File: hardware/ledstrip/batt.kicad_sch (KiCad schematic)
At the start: 37 parts, among them J4 BMS connectors, Q5 Q_NMOS, Q6 Q_NMOS, Q7 Q_NMOS, Q8 Q_NMOS, Q9 Q_PMOS, U5 BQ25703A

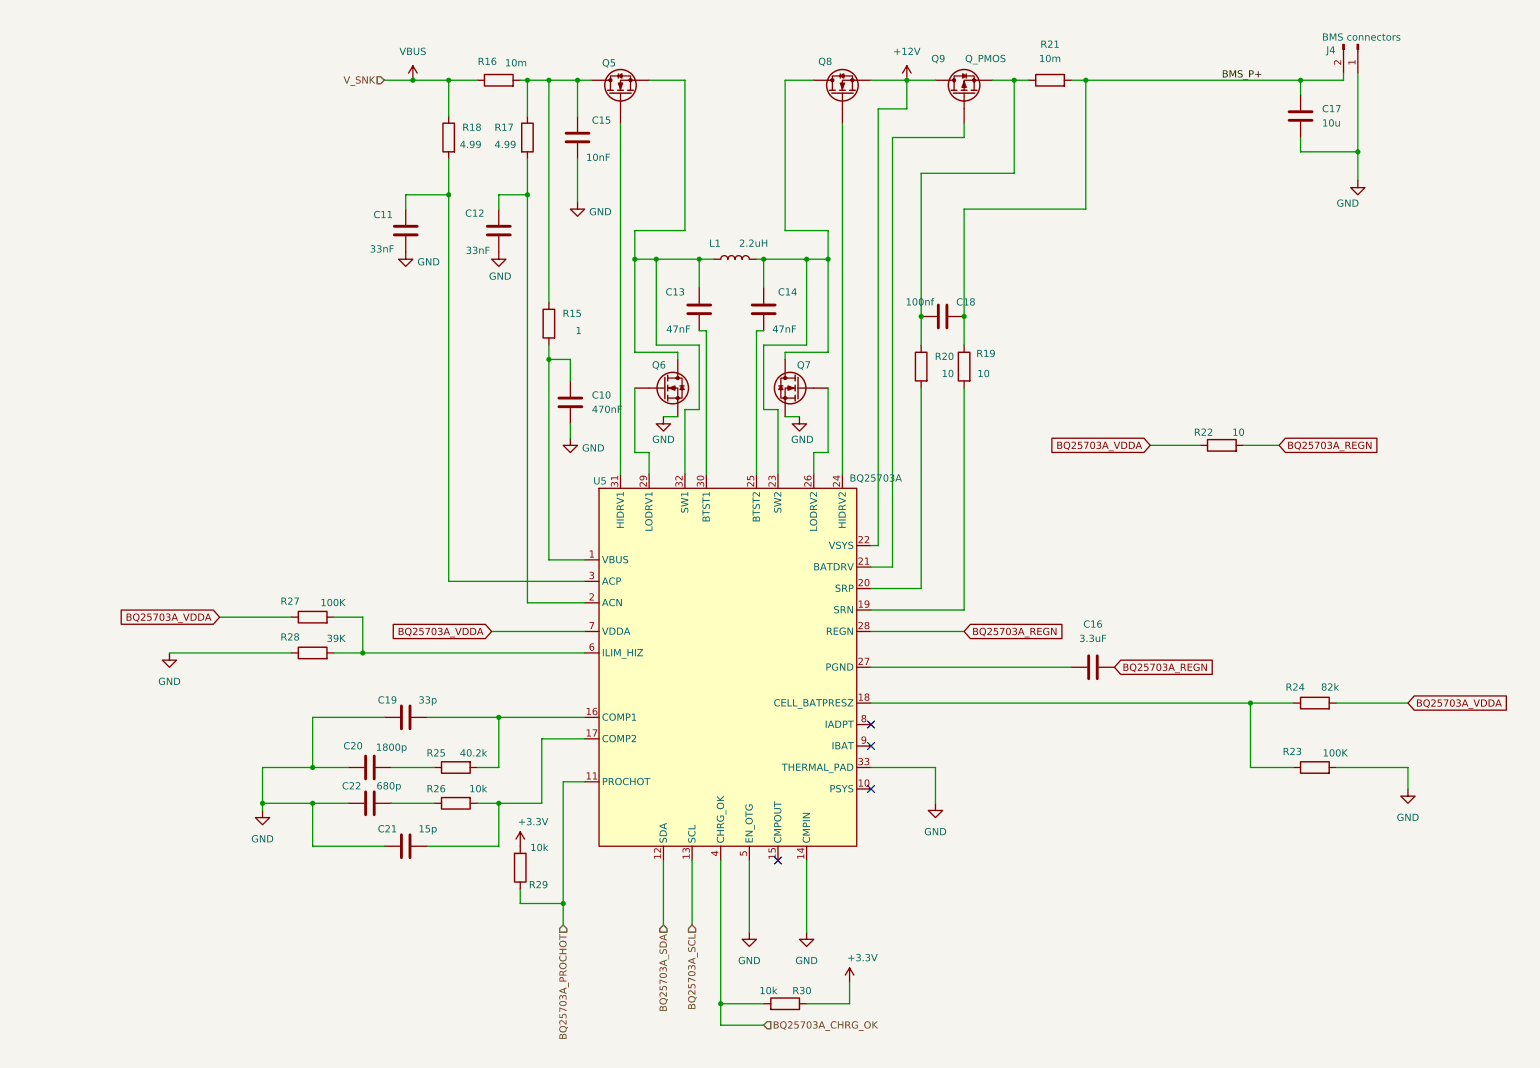
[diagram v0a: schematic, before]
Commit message: Fix ERC errors.
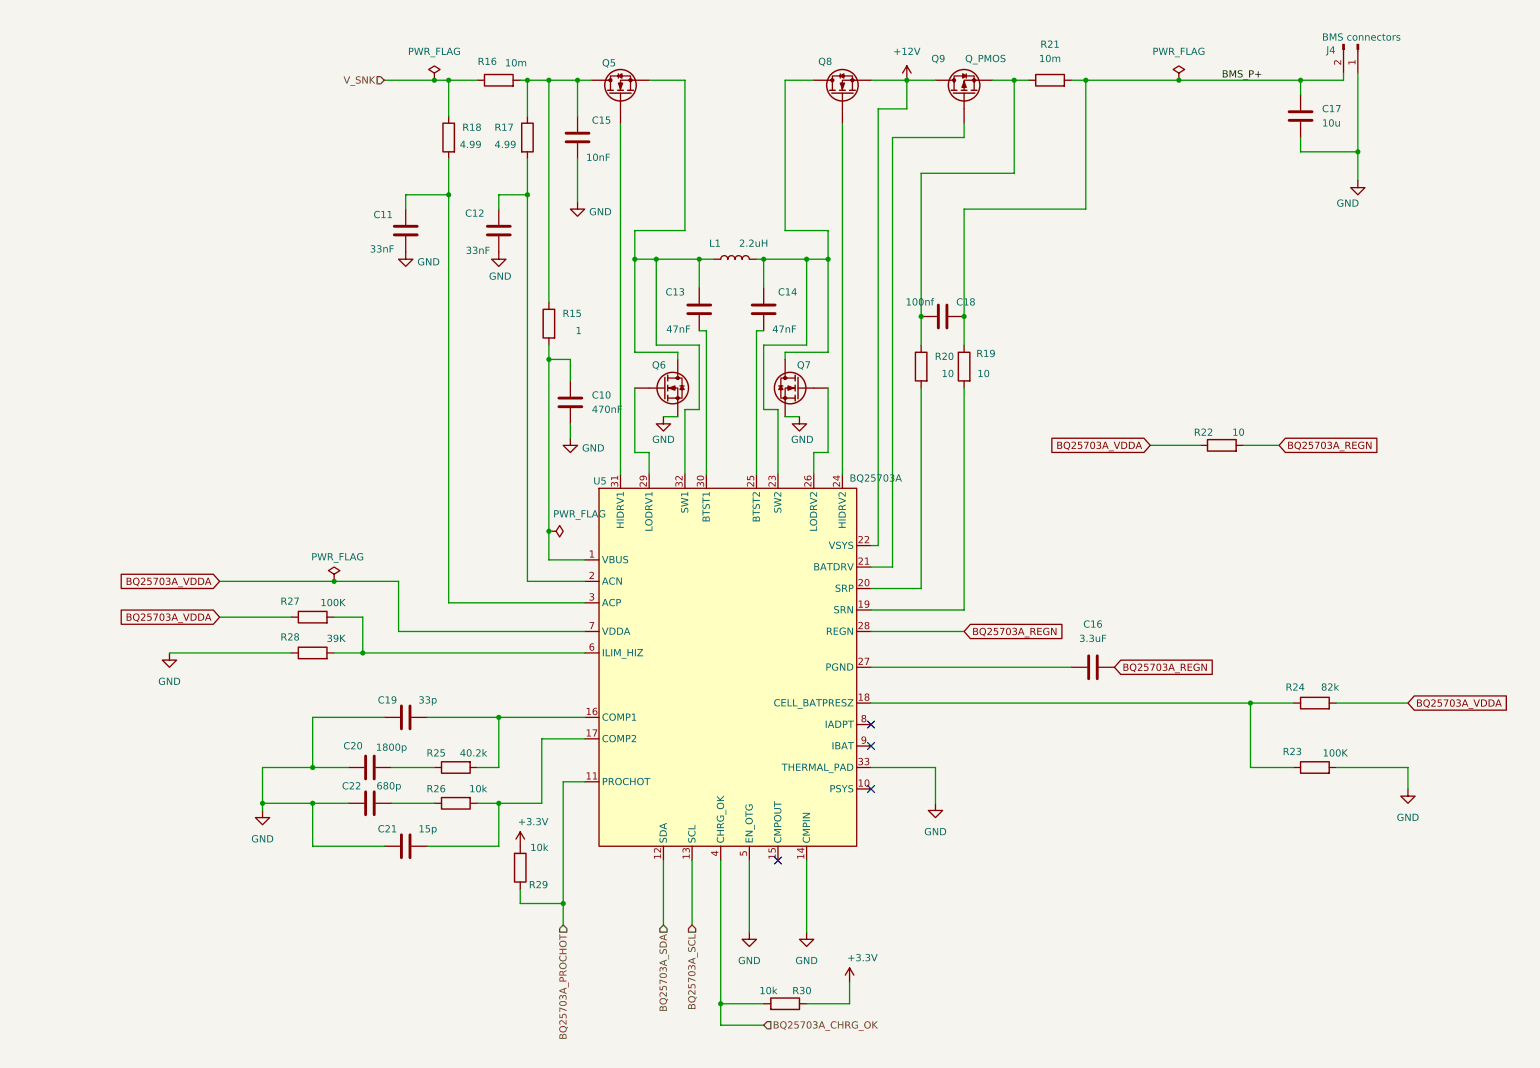
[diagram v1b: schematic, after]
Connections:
- net VBUS renamed V_SNK

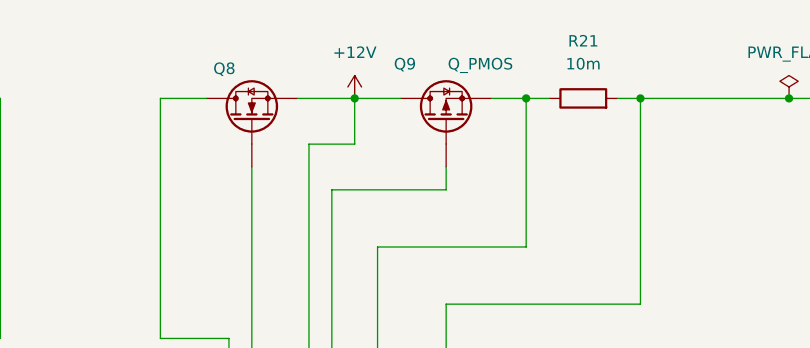
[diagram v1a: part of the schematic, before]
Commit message: Fix last errors in schematics
Missing footprint, missing distributor link.
Updated project sym-lib-table for ERC checks.
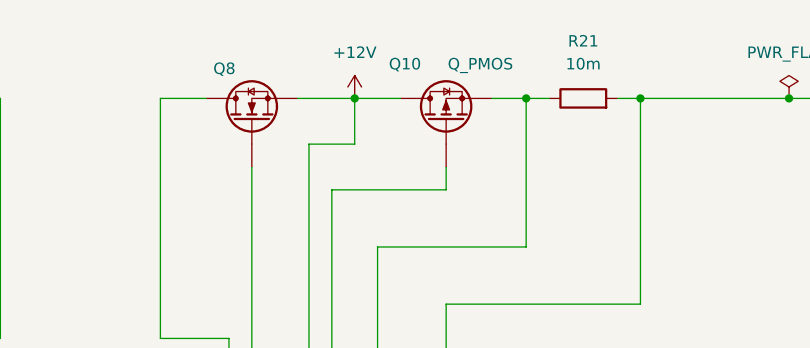
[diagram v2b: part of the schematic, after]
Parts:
- removed Q9: Q_PMOS, STL6P3LLH6:POWERFLAT_3P3X3P3_STM, symbol Device:Q_PMOS
- added Q10: Q_PMOS, STL6P3LLH6:POWERFLAT_3P3X3P3_STM, symbol Device:Q_PMOS
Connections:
- net +12V: now also Q10.D
- net at C18.1, R20.1, R21.1: now also Q10.S
- net at U5.21 (BATDRV): now also Q10.G
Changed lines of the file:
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@@
 		(on_board yes)
 		(dnp no)
-		(property "Reference" "Q9"
+		(property "Reference" "Q10"
 			(at 178.308 20.32 90)
 			(effects
@@
 			)
 		)
-		(property "Datasheet" "~"
+		(property "Datasheet" "https://www.st.com/resource/en/datasheet/stl6p3llh6.pdf"
 			(at 182.88 26.67 0)
 			(effects
@@
 			)
 		)
+		(property "Distributor Link 1" "https://www.mouser.com/ProductDetail/STMicroelectronics/STL6P3LLH6?qs=DqCdCwOw4%2F6Sn4l3cEaG7Q%3D%3D&srsltid=AfmBOor_CdWLVA3V0JAWOb-DG3H4EXYaOWWoltYAvPcJsUIQtpDcEfnR"
+			(at 182.88 26.67 90)
+			(effects
+				(font
+					(size 1.27 1.27)
+				)
+				(hide yes)
+			)
+		)
+		(property "Distributor Link 2" "https://www.digikey.com/en/products/detail/stmicroelectronics/STL6P3LLH6/5170838"
+			(at 182.88 26.67 90)
+			(effects
+				(font
+					(size 1.27 1.27)
+				)
+				(hide yes)
+			)
+		)
 		(pin "D"
 		)
@@
 			(project "ledstrip"
 				(path "/dcb997ee-94c4-4df2-ba22-0e091735ddd7/e1352532-a16b-4a34-87fb-bbe36c7f1290"
-					(reference "Q9")
+					(reference "Q10")
 					(unit 1)
 				)

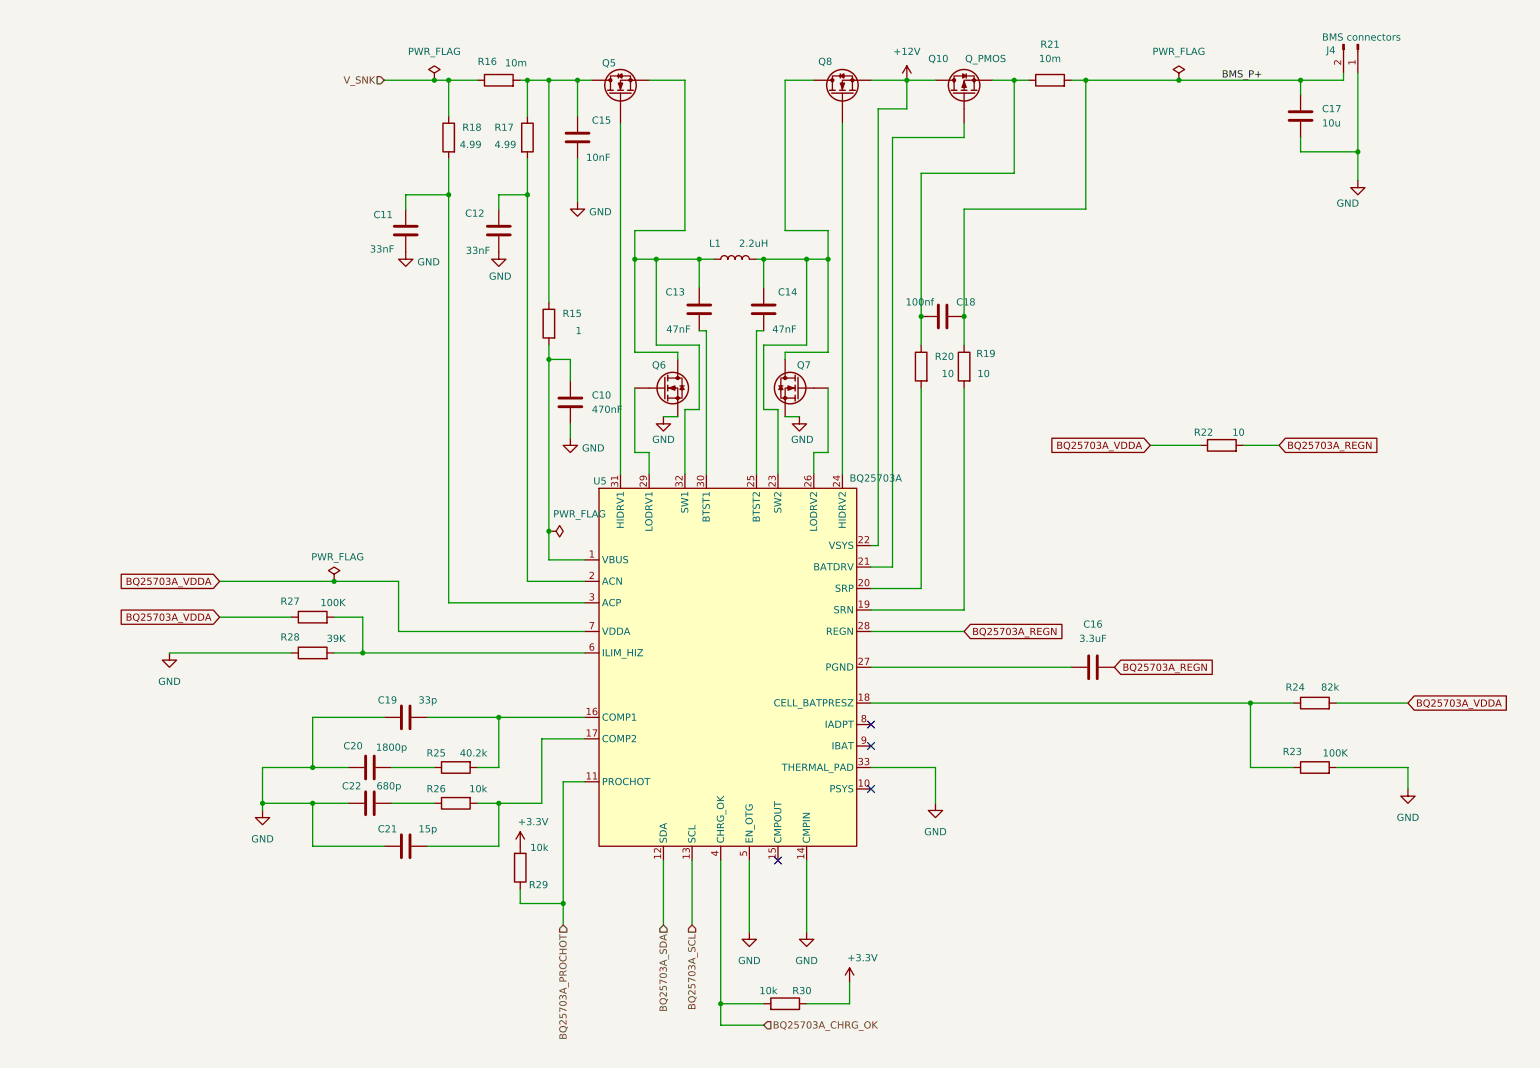
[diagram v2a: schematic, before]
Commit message: Add label on nodes.
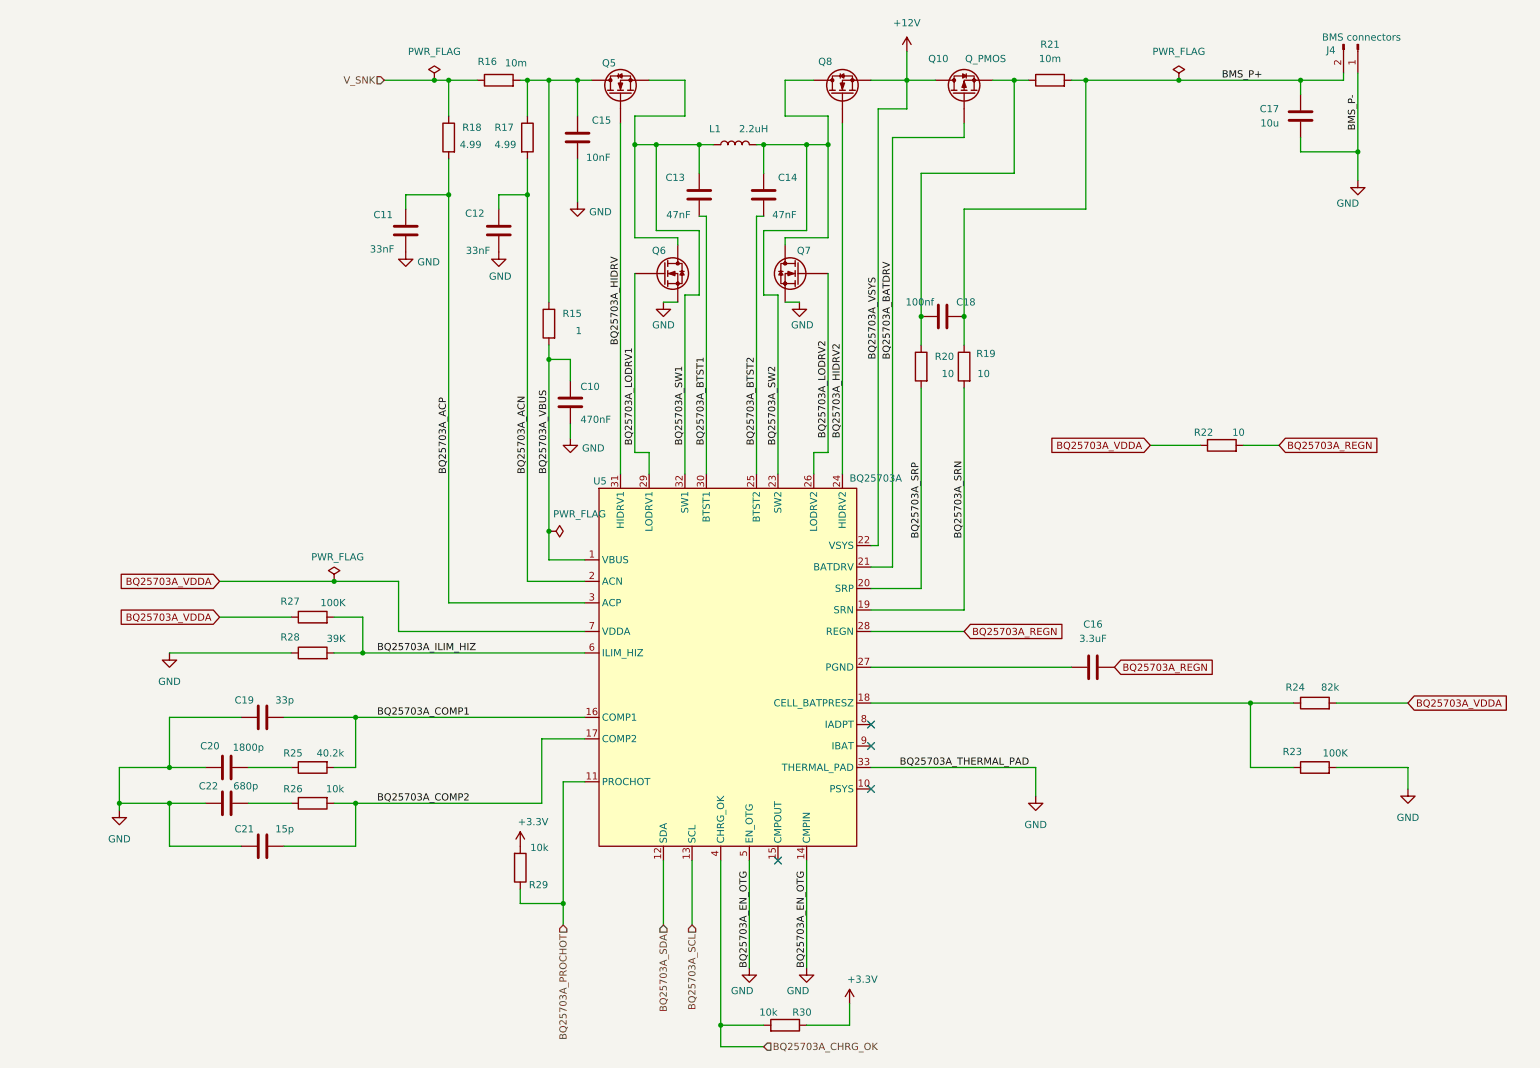
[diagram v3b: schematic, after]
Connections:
- net BQ25703A_BATDRV: now reaches Q10.G, U5.21 (BATDRV)
- net BQ25703A_SW2: now reaches C14.2, L1.2, Q7.D, Q8.D, U5.23 (SW2)
- net BQ25703A_HIDRV2: now reaches Q8.G, U5.24 (HIDRV2)
- net BQ25703A_SRP: now reaches R20.2, U5.20 (SRP)
- net BQ25703A_ACN: now reaches C12.2, R17.2, U5.2 (ACN)
- net BQ25703A_BTST1: now reaches C13.1, U5.30 (BTST1)
- net BQ25703A_SW1: now reaches C13.2, L1.1, Q5.S, Q6.D, U5.32 (SW1)
- net BQ25703A_VBUS: now reaches C10.2, R15.2, U5.1 (VBUS)
- net BQ25703A_SRN: now reaches R19.2, U5.19 (SRN)
- net BQ25703A_ILIM_HIZ: now reaches R27.2, R28.2, U5.6 (ILIM_HIZ)
- net BQ25703A_COMP1: now reaches C19.1, R25.2, U5.16 (COMP1)
- net BQ25703A_COMP2: now reaches C21.1, R26.2, U5.17 (COMP2)
- net BQ25703A_BTST2: now reaches C14.1, U5.25 (BTST2)
- net BQ25703A_LODRV2: now reaches Q7.G, U5.26 (LODRV2)
- net BQ25703A_LODRV1: now reaches Q6.G, U5.29 (LODRV1)
- net BQ25703A_ACP: now reaches C11.2, R18.2, U5.3 (ACP)
- net BQ25703A_HIDRV: now reaches Q5.G, U5.31 (HIDRV1)
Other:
- moved on the sheet: C13, C14, C19, C20, C21, C22, L1, Q6, Q7, R25, R26, R30

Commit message: Continue PCB.
Create netlists and color them.
Fix wrong symbol pin <-> foot print pins mapping.
Replace footprint and part for leds N-MOSFET.
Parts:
- Q5, Q6, Q7, Q8: footprint Package_SON:VSON-8_3.3x3.3mm_P0.65mm_NexFET -> NexFET:VSON-8_3.3x3.3mm_P0.65mm_NexFET
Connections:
- net BQ25703A_PGND: now reaches C16.2, U5.27 (PGND)
- net BQ25703A_CELL_BATPRESZ: now reaches R23.1, R24.1, U5.18 (CELL_BATPRESZ)
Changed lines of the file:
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@@
 	(wire
 		(pts
+			(xy 200.66 146.05) (xy 200.66 152.4)
+		)
+		(stroke
+			(width 0)
+			(type default)
+		)
+	)
+	(wire
+		(pts
 			(xy 166.37 118.11) (xy 182.88 118.11)
 		)
@@
 	(wire
 		(pts
-			(xy 166.37 146.05) (xy 195.58 146.05)
-		)
-		(stroke
-			(width 0)
-			(type default)
-		)
-	)
-	(wire
-		(pts
 			(xy 232.41 88.9) (xy 238.76 88.9)
 		)
@@
 	(wire
 		(pts
+			(xy 200.66 146.05) (xy 166.37 146.05)
+		)
+		(stroke
+			(width 0)
+			(type default)
+		)
+	)
+	(wire
+		(pts
 			(xy 88.9 24.13) (xy 91.44 24.13)
 		)
@@
 	(wire
 		(pts
-			(xy 195.58 146.05) (xy 195.58 151.13)
-		)
-		(stroke
-			(width 0)
-			(type default)
-		)
-	)
-	(wire
-		(pts
 			(xy 158.75 30.48) (xy 151.13 30.48)
 		)
@@
 	(wire
 		(pts
+			(xy 213.36 128.27) (xy 209.55 128.27)
+		)
+		(stroke
+			(width 0)
+			(type default)
+		)
+	)
+	(wire
+		(pts
 			(xy 172.72 29.21) (xy 172.72 24.13)
 		)
@@
 		)
 	)
+	(label "BQ25703A_PGND"
+		(at 176.53 128.27 0)
+		(effects
+			(font
+				(size 1.27 1.27)
+			)
+			(justify left bottom)
+		)
+	)
 	(label "BQ25703A_COMP2"
 		(at 78.74 152.4 0)
@@
 		)
 	)
+	(label "BQ25703A_CELL_BATPRESZ"
+		(at 182.88 134.62 0)
+		(effects
+			(font
+				(size 1.27 1.27)
+			)
+			(justify left bottom)
+		)
+	)
 	(label "BQ25703A_SW2"
 		(at 149.86 88.9 90)
@@
 	(global_label "BQ25703A_REGN"
 		(shape input)
-		(at 209.55 128.27 0)
+		(at 213.36 128.27 0)
 		(fields_autoplaced yes)
 		(effects
@@
 		)
 		(property "Intersheetrefs" "${INTERSHEET_REFS}"
-			(at 228.2589 128.27 0)
+			(at 232.0689 128.27 0)
 			(effects
 				(font
@@
 			)
 		)
-		(property "Footprint" "Package_SON:VSON-8_3.3x3.3mm_P0.65mm_NexFET"
+		(property "Footprint" "NexFET:VSON-8_3.3x3.3mm_P0.65mm_NexFET"
 			(at 158.75 21.59 0)
 			(effects
@@
 	(symbol
 		(lib_id "power:GND")
-		(at 195.58 151.13 0)
+		(at 200.66 152.4 0)
 		(unit 1)
 		(exclude_from_sim no)
@@
 		(fields_autoplaced yes)
 		(property "Reference" "#PWR035"
-			(at 195.58 157.48 0)
+			(at 200.66 158.75 0)
 			(effects
 				(font
@@
 		)
 		(property "Value" "GND"
-			(at 195.58 156.21 0)
+			(at 200.66 157.48 0)
 			(effects
 				(font
@@
 		)
 		(property "Footprint" ""
-			(at 195.58 151.13 0)
+			(at 200.66 152.4 0)
 			(effects
 				(font
@@
 		)
 		(property "Datasheet" ""
-			(at 195.58 151.13 0)
+			(at 200.66 152.4 0)
 			(effects
 				(font
@@
 		)
 		(property "Description" "Power symbol creates a global label with name \"GND\" , ground"
-			(at 195.58 151.13 0)
+			(at 200.66 152.4 0)
 			(effects
 				(font
@@
 			)
 		)
-		(property "Footprint" "Package_SON:VSON-8_3.3x3.3mm_P0.65mm_NexFET"
+		(property "Footprint" "NexFET:VSON-8_3.3x3.3mm_P0.65mm_NexFET"
 			(at 119.38 21.59 0)
 			(effects
@@
 			)
 		)
-		(property "Footprint" "Package_SON:VSON-8_3.3x3.3mm_P0.65mm_NexFET"
+		(property "Footprint" "NexFET:VSON-8_3.3x3.3mm_P0.65mm_NexFET"
 			(at 148.59 55.88 0)
 			(effects
@@
 			)
 		)
-		(property "Footprint" "Package_SON:VSON-8_3.3x3.3mm_P0.65mm_NexFET"
+		(property "Footprint" "NexFET:VSON-8_3.3x3.3mm_P0.65mm_NexFET"
 			(at 134.62 55.88 0)
 			(effects

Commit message: Fix ERC warnings.
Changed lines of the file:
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@@
-		)
-	)
-	(label "BQ25703A_EN_OTG"
-		(at 154.94 181.61 90)
-		(effects
-			(font
-				(size 1.27 1.27)
-			)
-			(justify left bottom)
-		)
-	)
-	(label "BQ25703A_EN_OTG"
-		(at 144.78 181.61 90)
-		(effects
-			(font
-				(size 1.27 1.27)
-			)
-			(justify left bottom)
 		)
 	)
@@
 		(effects
 			(font
-				(size 1.27 1.27)
-			)
-			(justify left bottom)
-		)
-	)
-	(label "BMS_P-"
-		(at 252.73 26.67 270)
-		(effects
-			(font
-				(size 1.27 1.27)
-			)
-			(justify right bottom)
-		)
-	)
-	(label "BQ25703A_THERMAL_PAD"
-		(at 171.45 146.05 0)
-		(effects
-			(font
-				(size 1.27 1.27)
-			)
-			(justify left bottom)
-		)
-	)
-	(label "BQ25703A_VSYS"
-		(at 167.64 73.66 90)
-		(effects
-			(font
